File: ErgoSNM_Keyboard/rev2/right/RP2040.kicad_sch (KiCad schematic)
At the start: 28 parts, among them SW1 BOOT, SW2 RESET, U3 W25Q128JVS, U4 RP2040, Y1 12MHz

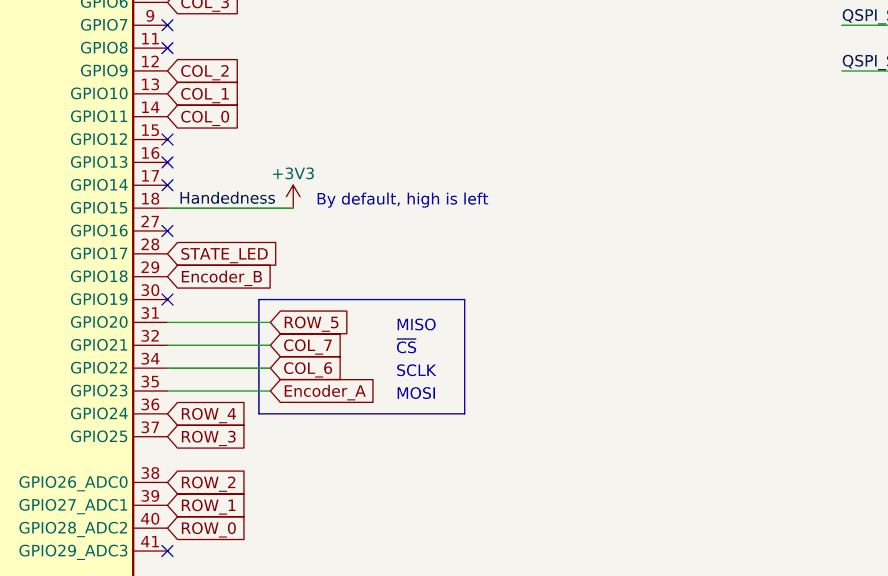
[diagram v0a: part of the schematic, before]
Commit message: Update right hand schematic
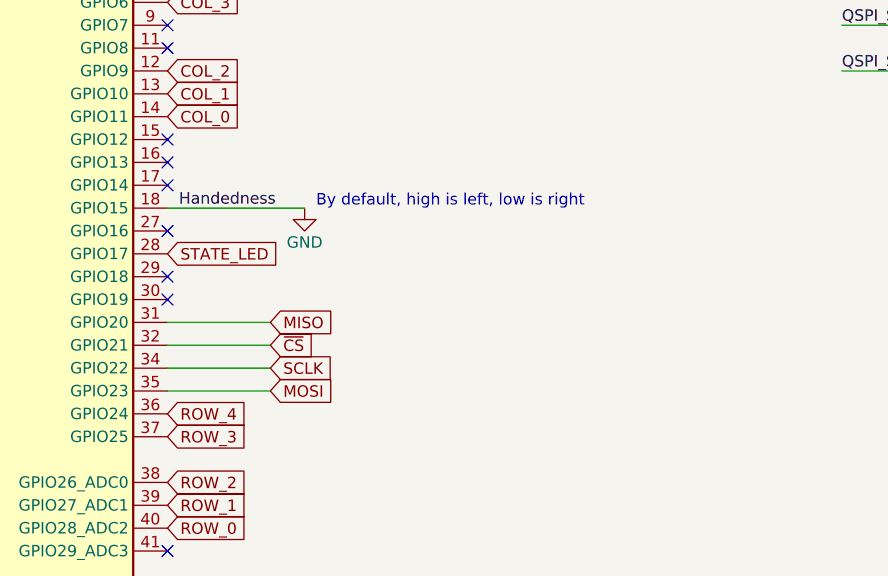
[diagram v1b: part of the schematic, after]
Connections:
- net +3V3: no longer U4.18 (GPIO15)
- net GND: now also U4.18 (GPIO15)
- net COL_6 renamed SCLK
- net COL_7 renamed ~{CS}
- net Encoder_A renamed MOSI
- net Encoder_B: no longer names the net of U4.29 (GPIO18)
- net ROW_5 renamed MISO
- no-connect marks 11 -> 12
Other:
- note added: "By default, high is left, low is right"
- note removed: "By default, high is left"
- note removed: "MISO"
- note removed: "MOSI"
- note removed: "SCLK"
- note removed: "~{CS}"
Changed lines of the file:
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@@
   (no_connect (at 114.3 41.91))
   (no_connect (at 114.3 39.37))
+  (no_connect (at 114.3 82.55))
   (wire (pts (xy 242.57 120.65) (xy 242.57 119.38))
     (stroke (width 0) (type default) (color 0 0 0 0))
@@
     (stroke (width 0) (type default) (color 0 0 0 0))
   )
-  (polyline (pts (xy 124.46 85.09) (xy 124.46 97.79))
-    (stroke (width 0) (type default) (color 0 0 0 0))
-  )
   (wire (pts (xy 116.84 34.29) (xy 116.84 36.83))
     (stroke (width 0) (type default) (color 0 0 0 0))
@@
     (stroke (width 0) (type default) (color 0 0 0 0))
   )
-  (wire (pts (xy 128.27 74.93) (xy 114.3 74.93))
+  (wire (pts (xy 129.54 74.93) (xy 114.3 74.93))
     (stroke (width 0) (type default) (color 0 0 0 0))
   )
@@
     (stroke (width 0) (type default) (color 0 0 0 0))
   )
-  (polyline (pts (xy 124.46 97.79) (xy 147.32 97.79))
-    (stroke (width 0) (type default) (color 0 0 0 0))
-  )
   (wire (pts (xy 99.06 25.4) (xy 99.06 26.67))
     (stroke (width 0) (type default) (color 0 0 0 0))
@@
     (stroke (width 0) (type default) (color 0 0 0 0))
   )
-  (polyline (pts (xy 147.32 97.79) (xy 147.32 85.09))
-    (stroke (width 0) (type default) (color 0 0 0 0))
-  )
   (wire (pts (xy 242.57 121.92) (xy 242.57 120.65))
     (stroke (width 0) (type default) (color 0 0 0 0))
@@
     (stroke (width 0) (type default) (color 0 0 0 0))
   )
-  (polyline (pts (xy 124.46 85.09) (xy 147.32 85.09))
-    (stroke (width 0) (type default) (color 0 0 0 0))
-  )
   (wire (pts (xy 203.2 120.65) (xy 212.09 120.65))
     (stroke (width 0) (type default) (color 0 0 0 0))
@@
   (wire (pts (xy 36.83 143.51) (xy 48.26 143.51))
     (stroke (width 0) (type default) (color 0 0 0 0))
-  )
-  (text "~{CS}" (at 139.7 91.44 0)
-    (effects (font (size 1.27 1.27)) (justify left bottom))
   )
   (text "Flash" (at 219.71 30.48 0)
     (effects (font (size 2 2) bold) (justify left bottom))
   )
-  (text "SCLK" (at 139.7 93.98 0)
-    (effects (font (size 1.27 1.27)) (justify left bottom))
-  )
-  (text "By default, high is left" (at 130.81 74.93 0)
-    (effects (font (size 1.27 1.27)) (justify left bottom))
-  )
-  (text "MISO" (at 139.7 88.9 0)
-    (effects (font (size 1.27 1.27)) (justify left bottom))
-  )
-  (text "MOSI" (at 139.7 96.52 0)
+  (text "By default, high is left, low is right" (at 130.81 74.93 0)
     (effects (font (size 1.27 1.27)) (justify left bottom))
   )
@@
     )
   )
-  (global_label "Encoder_A" (shape input) (at 125.73 95.25 0) (fields_autoplaced)
-    (effects (font (size 1.27 1.27)) (justify left))
-    (property "Intersheet References" "${INTERSHEET_REFS}" (id 0) (at 137.7588 95.1706 0)
-      (effects (font (size 1.27 1.27)) (justify left) hide)
-    )
-  )
-  (global_label "COL_6" (shape input) (at 125.73 92.71 0) (fields_autoplaced)
-    (effects (font (size 1.27 1.27)) (justify left))
-    (property "Intersheet References" "${INTERSHEET_REFS}" (id 0) (at 133.9488 92.6306 0)
-      (effects (font (size 1.27 1.27)) (justify left) hide)
-    )
-  )
-  (global_label "COL_7" (shape input) (at 125.73 90.17 0) (fields_autoplaced)
-    (effects (font (size 1.27 1.27)) (justify left))
-    (property "Intersheet References" "${INTERSHEET_REFS}" (id 0) (at 133.9488 90.0906 0)
+  (global_label "MOSI" (shape input) (at 125.73 95.25 0) (fields_autoplaced)
+    (effects (font (size 1.27 1.27)) (justify left))
+    (property "Intersheet References" "${INTERSHEET_REFS}" (id 0) (at 132.7393 95.1706 0)
+      (effects (font (size 1.27 1.27)) (justify left) hide)
+    )
+  )
+  (global_label "SCLK" (shape input) (at 125.73 92.71 0) (fields_autoplaced)
+    (effects (font (size 1.27 1.27)) (justify left))
+    (property "Intersheet References" "${INTERSHEET_REFS}" (id 0) (at 132.9207 92.6306 0)
+      (effects (font (size 1.27 1.27)) (justify left) hide)
+    )
+  )
+  (global_label "~{CS}" (shape input) (at 125.73 90.17 0) (fields_autoplaced)
+    (effects (font (size 1.27 1.27)) (justify left))
+    (property "Intersheet References" "${INTERSHEET_REFS}" (id 0) (at 130.6226 90.0906 0)
       (effects (font (size 1.27 1.27)) (justify left) hide)
     )
@@
     )
   )
-  (global_label "Encoder_B" (shape input) (at 114.3 82.55 0) (fields_autoplaced)
-    (effects (font (size 1.27 1.27)) (justify left))
-    (property "Intersheet References" "${INTERSHEET_REFS}" (id 0) (at 126.5102 82.4706 0)
-      (effects (font (size 1.27 1.27)) (justify left) hide)
-    )
-  )
   (global_label "STATE_LED" (shape input) (at 114.3 80.01 0) (fields_autoplaced)
     (effects (font (size 1.27 1.27)) (justify left))
@@
     )
   )
-  (global_label "ROW_5" (shape input) (at 125.73 87.63 0) (fields_autoplaced)
-    (effects (font (size 1.27 1.27)) (justify left))
-    (property "Intersheet References" "${INTERSHEET_REFS}" (id 0) (at 134.3721 87.5506 0)
+  (global_label "MISO" (shape input) (at 125.73 87.63 0) (fields_autoplaced)
+    (effects (font (size 1.27 1.27)) (justify left))
+    (property "Intersheet References" "${INTERSHEET_REFS}" (id 0) (at 132.7393 87.5506 0)
       (effects (font (size 1.27 1.27)) (justify left) hide)
     )
@@
     (pin "1")
     (pin "2")
+  )
+  (symbol (lib_id "power:GND") (at 129.54 74.93 0) (unit 1)
+    (in_bom yes) (on_board yes)
+    (property "Reference" "#PWR?" (id 0) (at 129.54 81.28 0)
+      (effects (font (size 1.27 1.27)) hide)
+    )
+    (property "Value" "GND" (id 1) (at 129.54 78.74 0))
+    (property "Footprint" "" (id 2) (at 129.54 74.93 0)
+      (effects (font (size 1.27 1.27)) hide)
+    )
+    (property "Datasheet" "" (id 3) (at 129.54 74.93 0)
+      (effects (font (size 1.27 1.27)) hide)
+    )
+    (pin "1")
   )
   (symbol (lib_id "Device:C") (at 71.12 170.18 0) (unit 1)
@@
     (pin "2")
   )
-  (symbol (lib_id "power:+3V3") (at 128.27 74.93 0) (unit 1)
-    (in_bom yes) (on_board yes)
-    (property "Reference" "#PWR028" (id 0) (at 128.27 78.74 0)
-      (effects (font (size 1.27 1.27)) hide)
-    )
-    (property "Value" "+3V3" (id 1) (at 128.27 71.12 0))
-    (property "Footprint" "" (id 2) (at 128.27 74.93 0)
-      (effects (font (size 1.27 1.27)) hide)
-    )
-    (property "Datasheet" "" (id 3) (at 128.27 74.93 0)
-      (effects (font (size 1.27 1.27)) hide)
-    )
-    (pin "1")
-  )
 )
